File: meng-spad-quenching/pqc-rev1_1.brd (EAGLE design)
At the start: 76.2 x 50.8 mm, 54 parts, among them IC1 ADCMP582, IC3 LT3032-5, J1 VIN_LOGIC, U1 SN65EPT21DGK, U2 TPS78233DDCT, U3 SN65EPT22DGK, X1 CONN_SPAD, X2 CONN_SCOPE_COMP, X3 CONN_SCOPE_RSHUNT, X4 CONN_VA_BIAS, X5 CONN_LATCH_IN

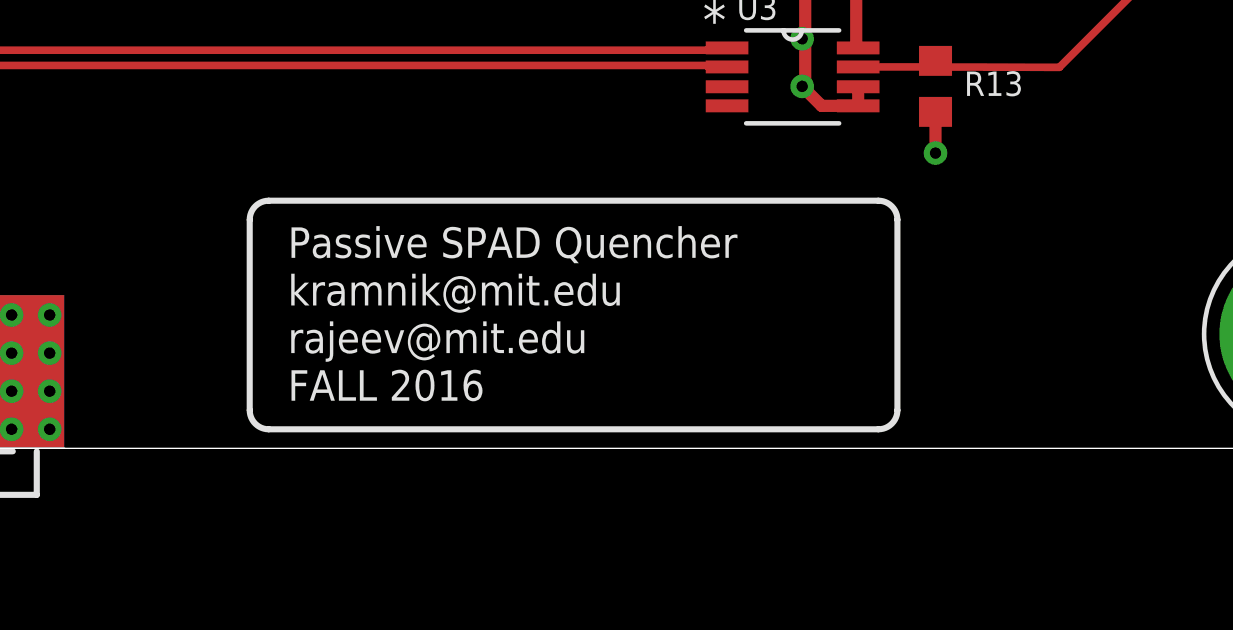
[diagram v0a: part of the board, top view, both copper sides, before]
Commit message: Moved to PQC rev. 1.1 --- fixed hysteresis resistor connection.
Hysteresis resistor (R3) should be connected to comparator negative
supply rail, not GND. Re-exported Gerbers.
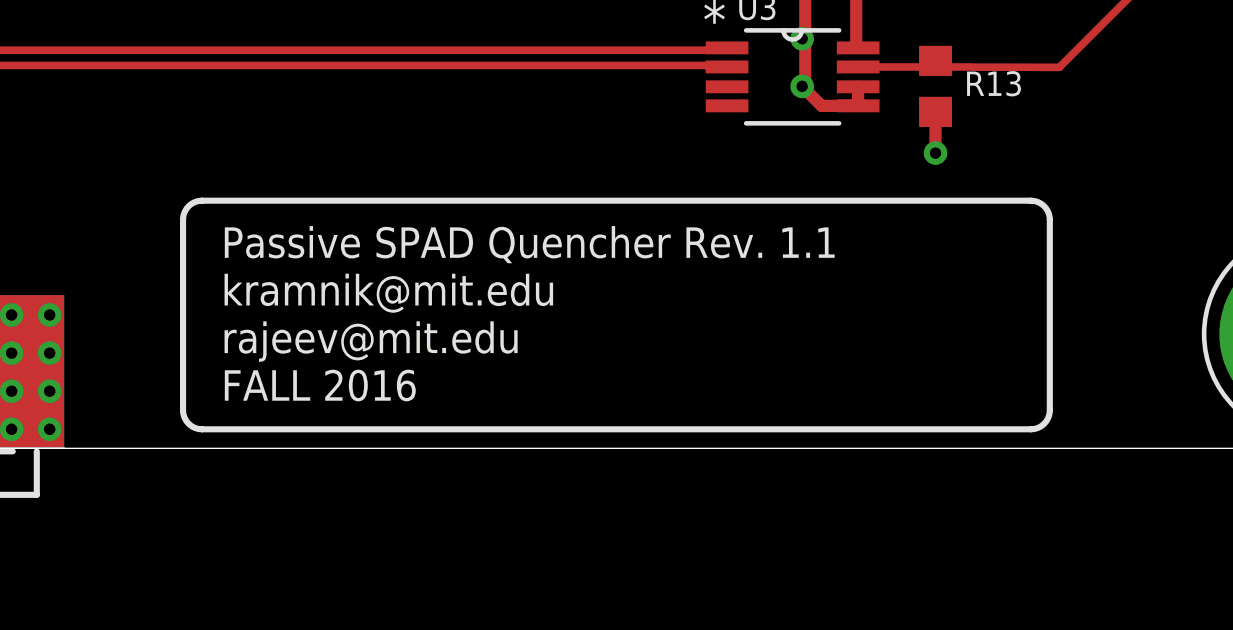
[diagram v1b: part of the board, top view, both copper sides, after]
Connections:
- net GND: no longer R3.1
- net PP_N5V0: now also R3.1
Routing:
- net GND: track 69.9 -> 68.3 mm, vias 112 -> 111
- net PP_N5V0: track 7.98 -> 9.57 mm, vias 4 -> 5
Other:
- board text added: "Passive SPAD Quencher Rev. 1.1"
- board text removed: "Passive SPAD Quencher"
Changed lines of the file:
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@@
 <text x="64.77" y="46.6725" size="1.016" layer="21" font="vector" ratio="16" rot="R90">VIN-</text>
 <text x="60.6425" y="46.6725" size="1.016" layer="21" font="vector" ratio="16" rot="R90">GND</text>
-<text x="38.4175" y="6.35" size="1.016" layer="21" font="vector" ratio="16">Passive SPAD Quencher</text>
-<text x="38.4175" y="4.7625" size="1.016" layer="21" font="vector" ratio="16">kramnik@mit.edu</text>
-<text x="38.4175" y="1.5875" size="1.016" layer="21" font="vector" ratio="16">FALL 2016</text>
-<text x="38.4175" y="3.175" size="1.016" layer="21" font="vector" ratio="16">rajeev@mit.edu</text>
-<wire x1="37.1475" y1="7.62" x2="37.1475" y2="1.27" width="0.2032" layer="21"/>
-<wire x1="37.1475" y1="1.27" x2="37.7825" y2="0.635" width="0.2032" layer="21" curve="90"/>
-<wire x1="37.7825" y1="0.635" x2="58.1025" y2="0.635" width="0.2032" layer="21"/>
-<wire x1="58.1025" y1="0.635" x2="58.7375" y2="1.27" width="0.2032" layer="21" curve="90"/>
-<wire x1="58.7375" y1="1.27" x2="58.7375" y2="7.62" width="0.2032" layer="21"/>
-<wire x1="58.7375" y1="7.62" x2="58.1025" y2="8.255" width="0.2032" layer="21" curve="90"/>
-<wire x1="58.1025" y1="8.255" x2="37.7825" y2="8.255" width="0.2032" layer="21"/>
-<wire x1="37.7825" y1="8.255" x2="37.1475" y2="7.62" width="0.2032" layer="21" curve="90"/>
+<text x="36.195" y="6.35" size="1.016" layer="21" font="vector" ratio="16">Passive SPAD Quencher Rev. 1.1</text>
+<text x="36.195" y="4.7625" size="1.016" layer="21" font="vector" ratio="16">kramnik@mit.edu</text>
+<text x="36.195" y="1.5875" size="1.016" layer="21" font="vector" ratio="16">FALL 2016</text>
+<text x="36.195" y="3.175" size="1.016" layer="21" font="vector" ratio="16">rajeev@mit.edu</text>
+<wire x1="34.925" y1="7.62" x2="34.925" y2="1.27" width="0.2032" layer="21"/>
+<wire x1="34.925" y1="1.27" x2="35.56" y2="0.635" width="0.2032" layer="21" curve="90"/>
+<wire x1="35.56" y1="0.635" x2="63.1825" y2="0.635" width="0.2032" layer="21"/>
+<wire x1="63.1825" y1="0.635" x2="63.8175" y2="1.27" width="0.2032" layer="21" curve="90"/>
+<wire x1="63.8175" y1="1.27" x2="63.8175" y2="7.62" width="0.2032" layer="21"/>
+<wire x1="63.8175" y1="7.62" x2="63.1825" y2="8.255" width="0.2032" layer="21" curve="90"/>
+<wire x1="63.1825" y1="8.255" x2="35.56" y2="8.255" width="0.2032" layer="21"/>
+<wire x1="35.56" y1="8.255" x2="34.925" y2="7.62" width="0.2032" layer="21" curve="90"/>
 <text x="54.2925" y="34.925" size="1.016" layer="21" font="vector" ratio="16">+/-15V Max.</text>
 <text x="5.715" y="25.0825" size="1.016" layer="21" font="vector" ratio="16">+VA</text>
@@
 <contactref element="IC1" pad="4"/>
 <contactref element="R2" pad="1"/>
-<contactref element="R3" pad="1"/>
 <contactref element="X1" pad="G@1"/>
 <contactref element="X3" pad="G@1"/>
@@
 <vertex x="0" y="50.8"/>
 </polygon>
-<via x="22.86" y="29.21" extent="1-16" drill="0.381"/>
 <via x="40.3225" y="33.3375" extent="1-16" drill="0.381"/>
 <contactref element="U1" pad="5"/>
@@
 <wire x1="36.2204" y1="27.0002" x2="38.3277" y2="27.0002" width="0.4064" layer="1"/>
 <wire x1="38.3277" y1="27.0002" x2="38.4175" y2="27.09" width="0.4064" layer="1"/>
-<wire x1="21.27" y1="29.21" x2="22.86" y2="29.21" width="0.4064" layer="1"/>
 <via x="25.0825" y="16.8275" extent="1-16" drill="0.381"/>
 <wire x1="24.765" y1="19.05" x2="23.3925" y2="19.05" width="0.4064" layer="1"/>
@@
 <wire x1="22.645" y1="24.2325" x2="22.86" y2="24.4475" width="0.4064" layer="1"/>
 <contactref element="TP2" pad="TP"/>
+<contactref element="R3" pad="1"/>
+<via x="22.86" y="29.21" extent="1-16" drill="0.381"/>
+<wire x1="21.27" y1="29.21" x2="22.86" y2="29.21" width="0.4064" layer="1"/>
 </signal>
 <signal name="PP_P5V0">

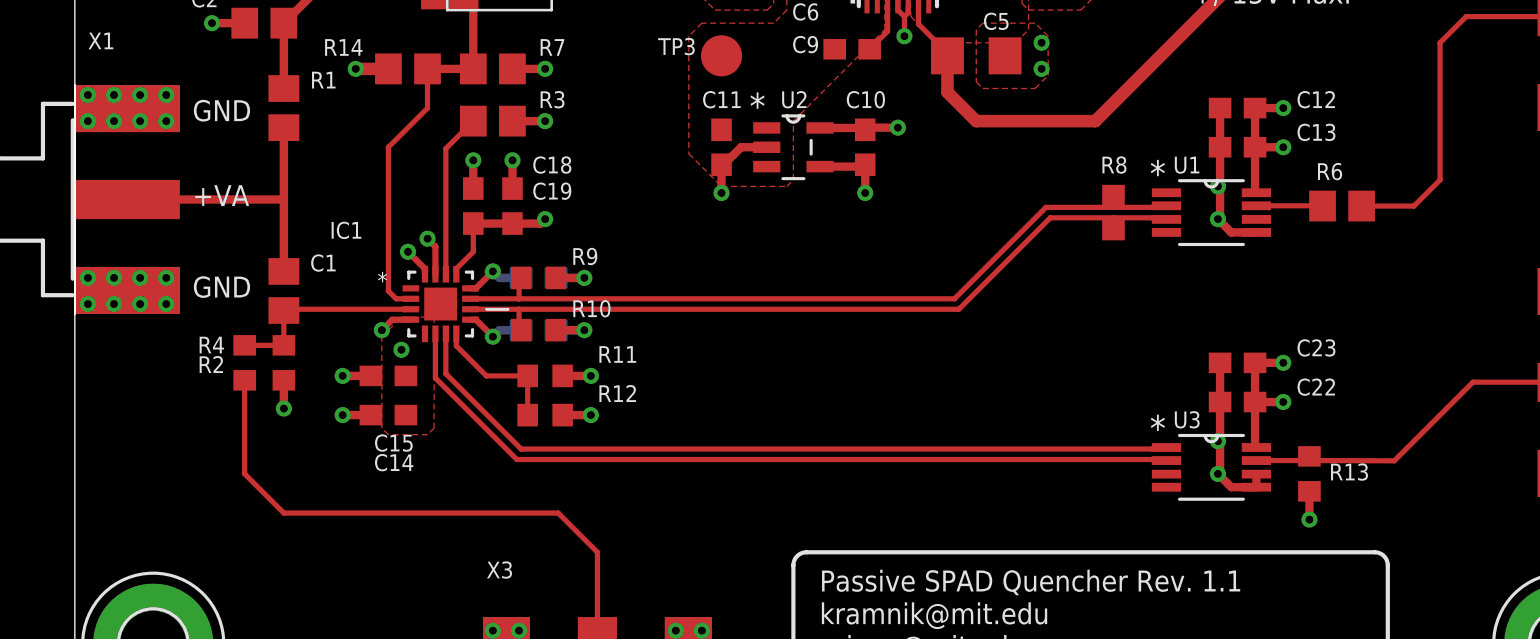
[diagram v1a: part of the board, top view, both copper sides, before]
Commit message: Fixed some lingering bugs
Removed T-termination pullup (not necessary). Flipped LATCH polarity so
SMA is active-high and can be left floating.
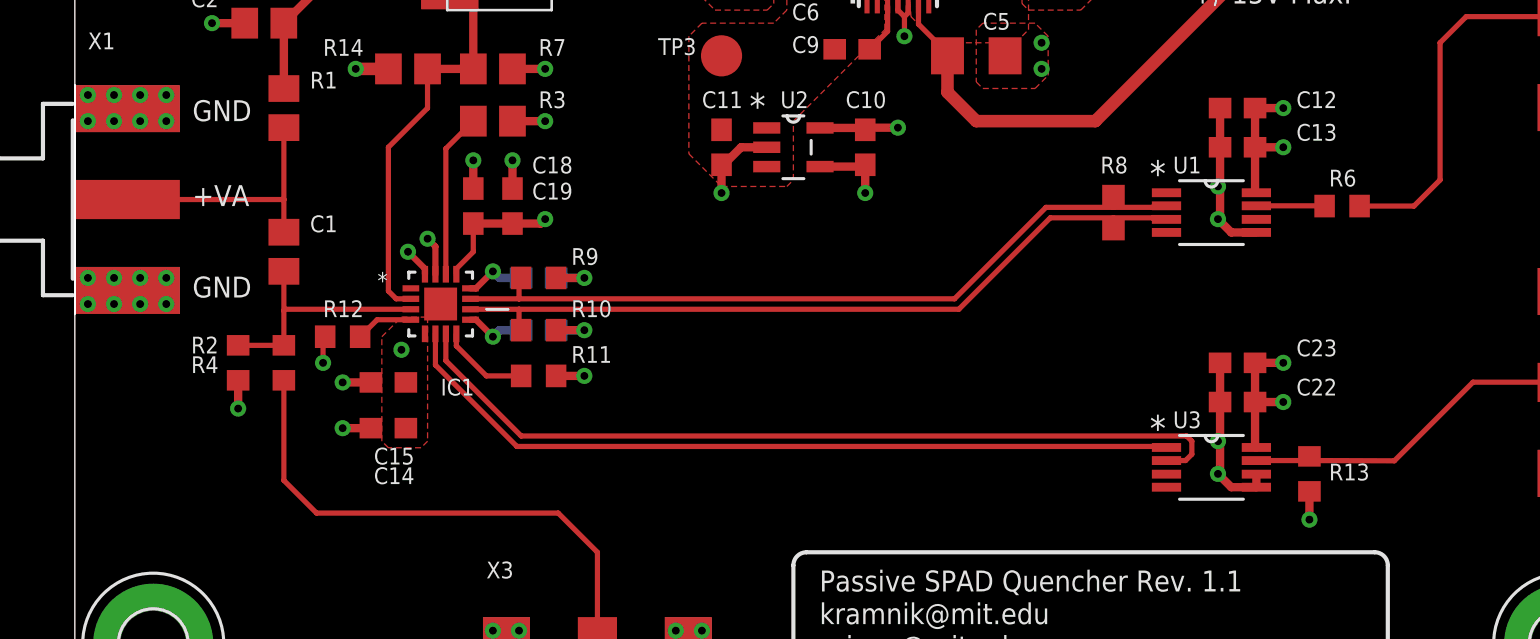
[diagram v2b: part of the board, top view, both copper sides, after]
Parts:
- R4: value DNP -> 0R
- R6: device rcl:R0805 -> rcl:R0603
- moved R12 10.6 mm to (13.0, 18.7), turned to 0 degrees
- moved R2 2.22 mm to (7.94, 17.5)
- moved C1 1.91 mm to (10.2, 22.9)
- moved R4 1.90 mm to (10.2, 17.5)
- moved C14 0.63 mm to (15.2, 14.3)
- moved C15 0.32 mm to (15.2, 16.5)
- moved R11 0.32 mm to (22.5, 16.8)
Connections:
- new net N$3: IC1.4, R12.2
- net COMP_LE_N: now also U3.1; no longer U3.2
- net COMP_LE_P: now also U3.2; no longer U3.1
- net GND: now also R12.1; no longer IC1.4
- net N$6: no longer R12.2
- net PP_P3V3: no longer R12.1
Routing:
- net N$3: track 0.00 -> 2.81 mm
- net COMP_LE_P: track 38.5 -> 41.2 mm
- net VCOMP_IN: track 9.79 -> 12.0 mm
- net N$6: track 6.56 -> 4.34 mm
- net VSPAD: track 14.6 -> 12.7 mm
- net VSCOPE_1: track 29.0 -> 27.2 mm
- net PP_P3V3: track 24.7 -> 23.3 mm, vias 8 -> 7
- net COMP_LE_N: track 39.3 -> 38.7 mm
